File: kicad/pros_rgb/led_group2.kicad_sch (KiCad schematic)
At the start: 4 parts

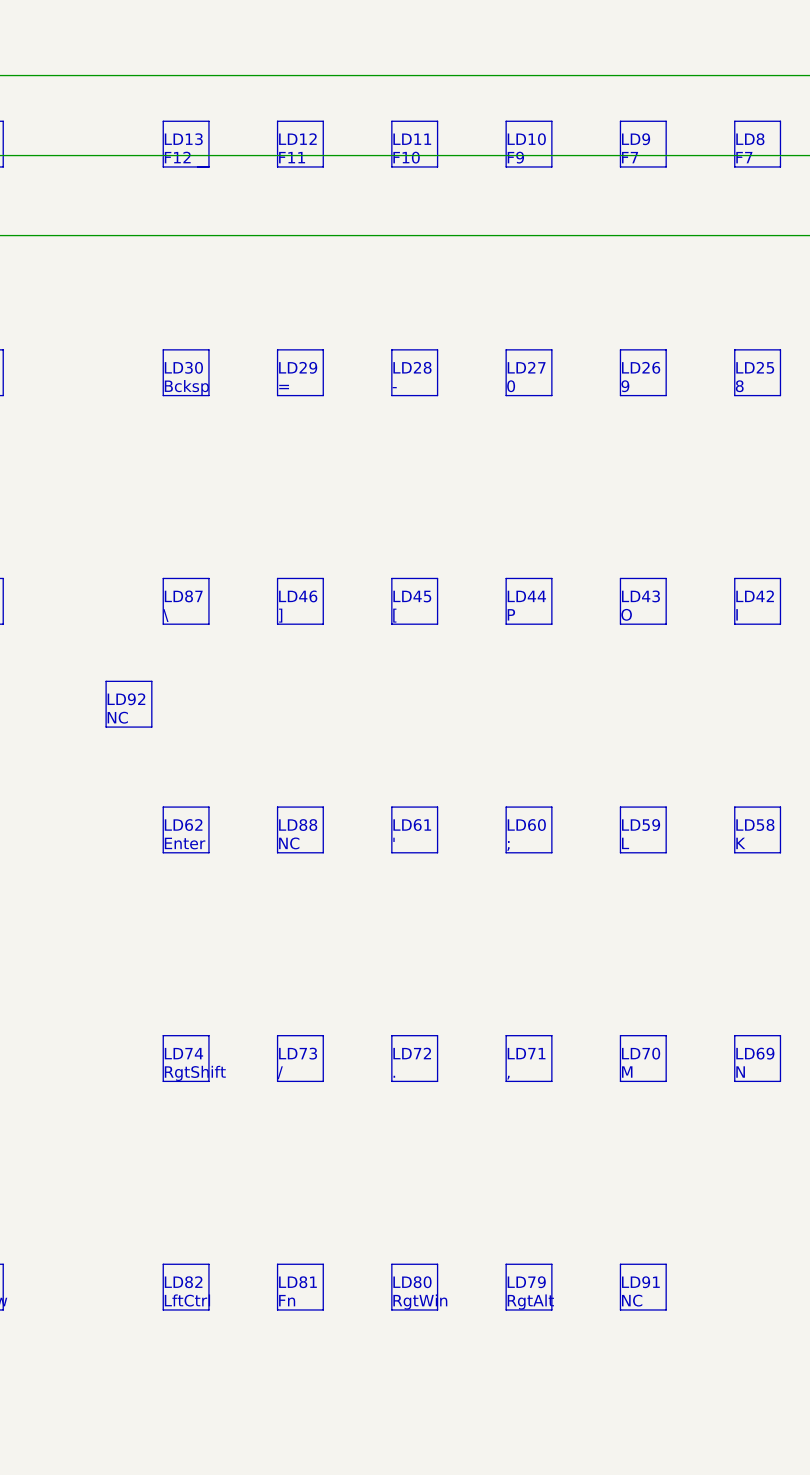
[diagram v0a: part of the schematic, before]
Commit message: kicad/pros_rgb: fix typos
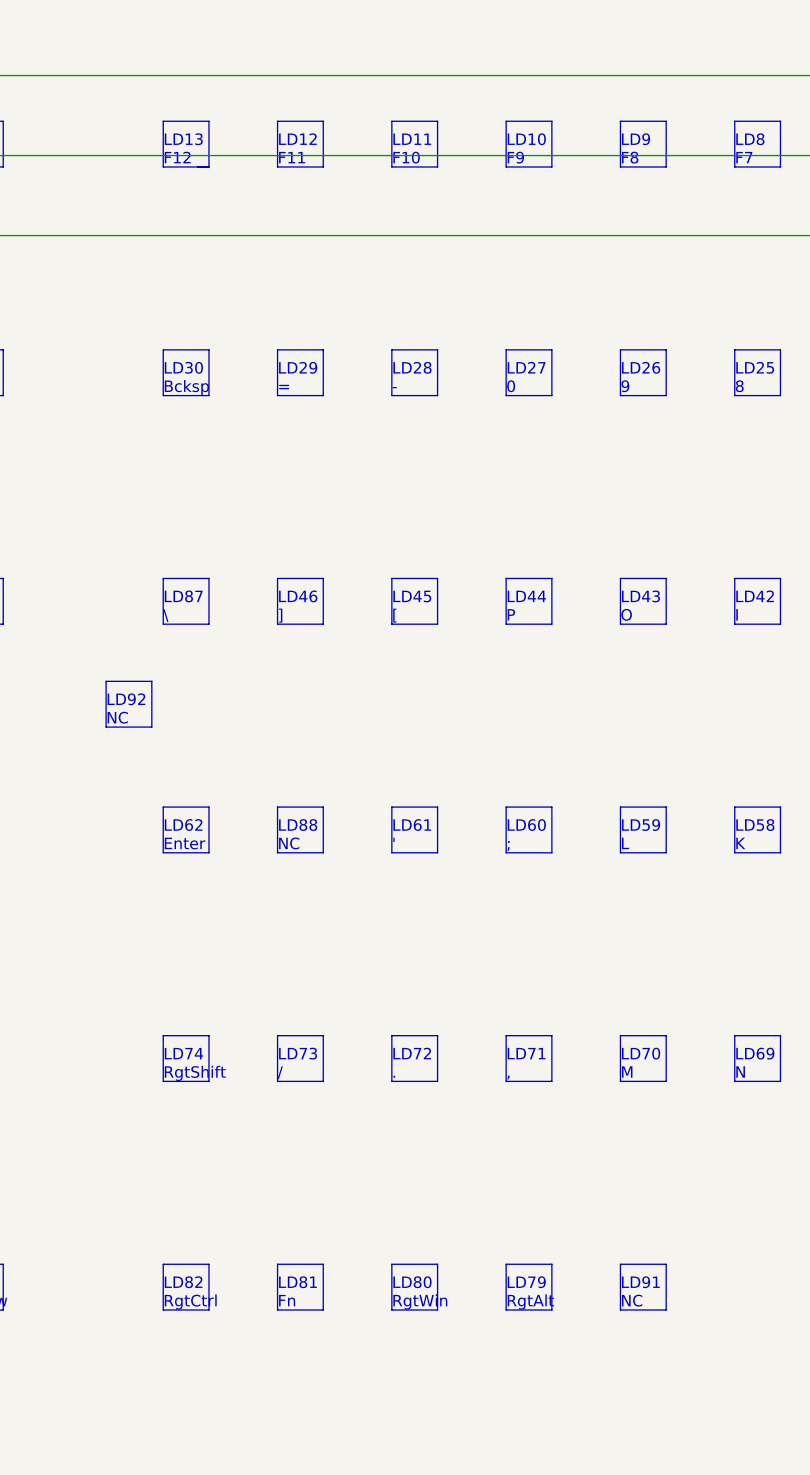
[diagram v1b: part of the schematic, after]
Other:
- note added: "LD82 RgtCtrl"
- note added: "LD9 F8"
- note removed: "LD82 LftCtrl"
- note removed: "LD9 F7"
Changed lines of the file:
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@@
     (effects (font (size 1.27 1.27)) (justify left bottom))
   )
-  (text "LD82\nLftCtrl" (at 106.68 156.21 0)
+  (text "LD82\nRgtCtrl" (at 106.68 156.21 0)
     (effects (font (size 1.27 1.27)) (justify left bottom))
   )
@@
     (effects (font (size 1.27 1.27)) (justify left bottom))
   )
-  (text "LD9\nF7" (at 157.48 29.21 0)
+  (text "LD9\nF8" (at 157.48 29.21 0)
     (effects (font (size 1.27 1.27)) (justify left bottom))
   )

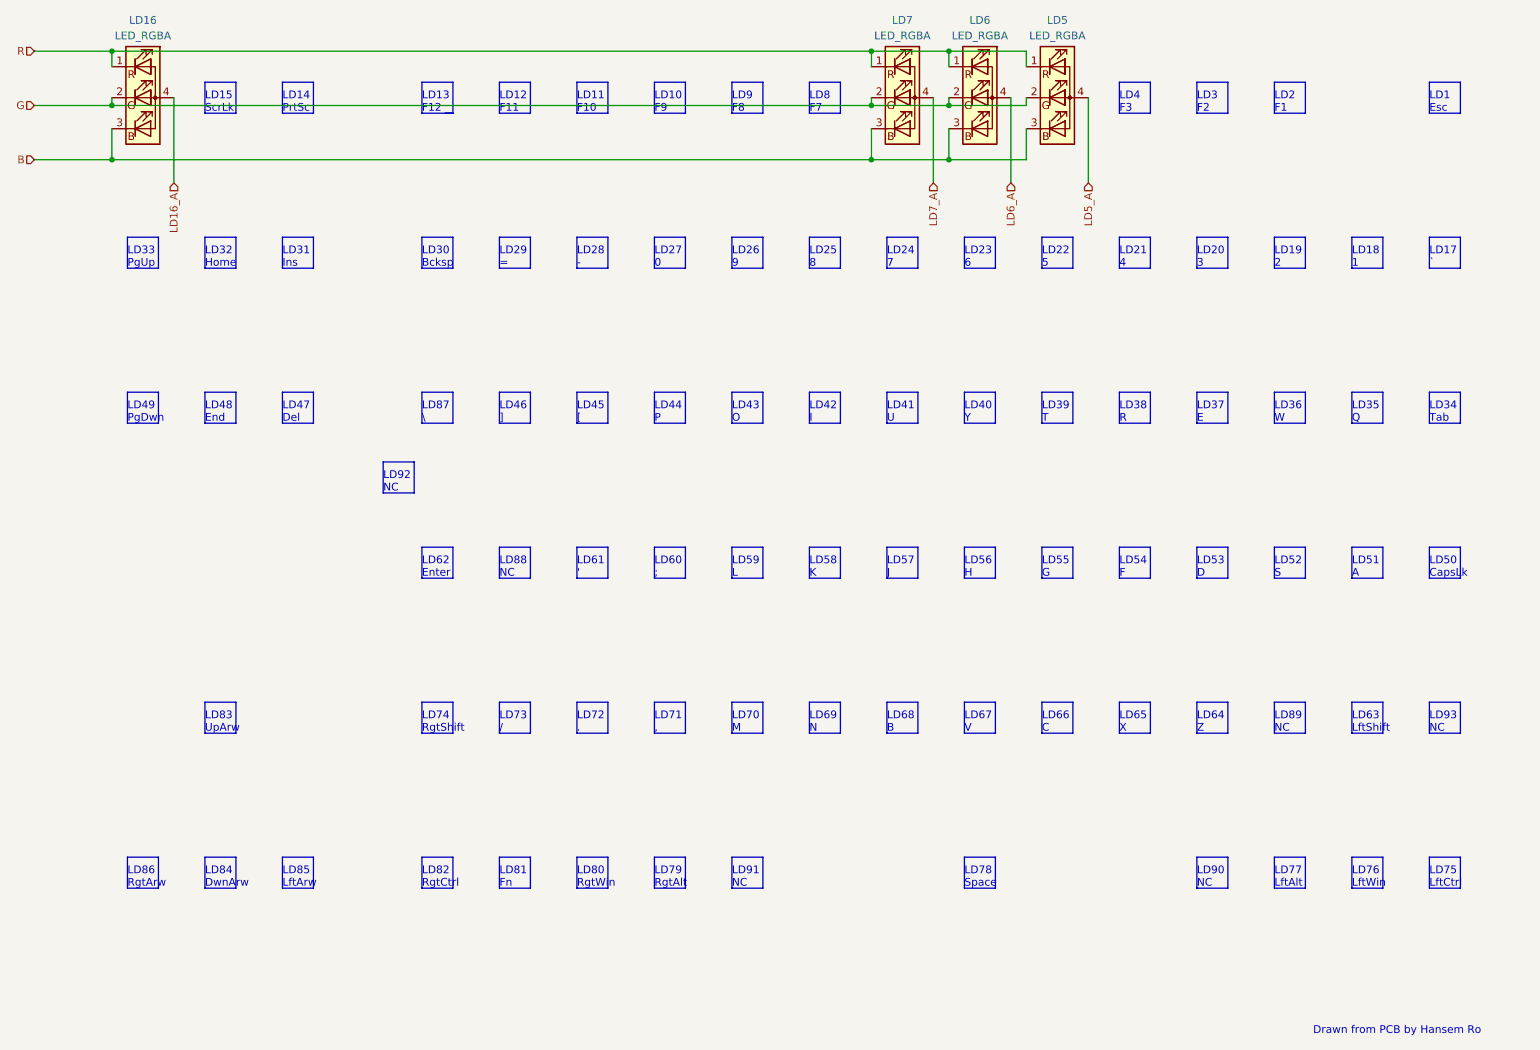
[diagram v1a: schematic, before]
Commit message: kicad/pros_rgb: order led groups by channel number
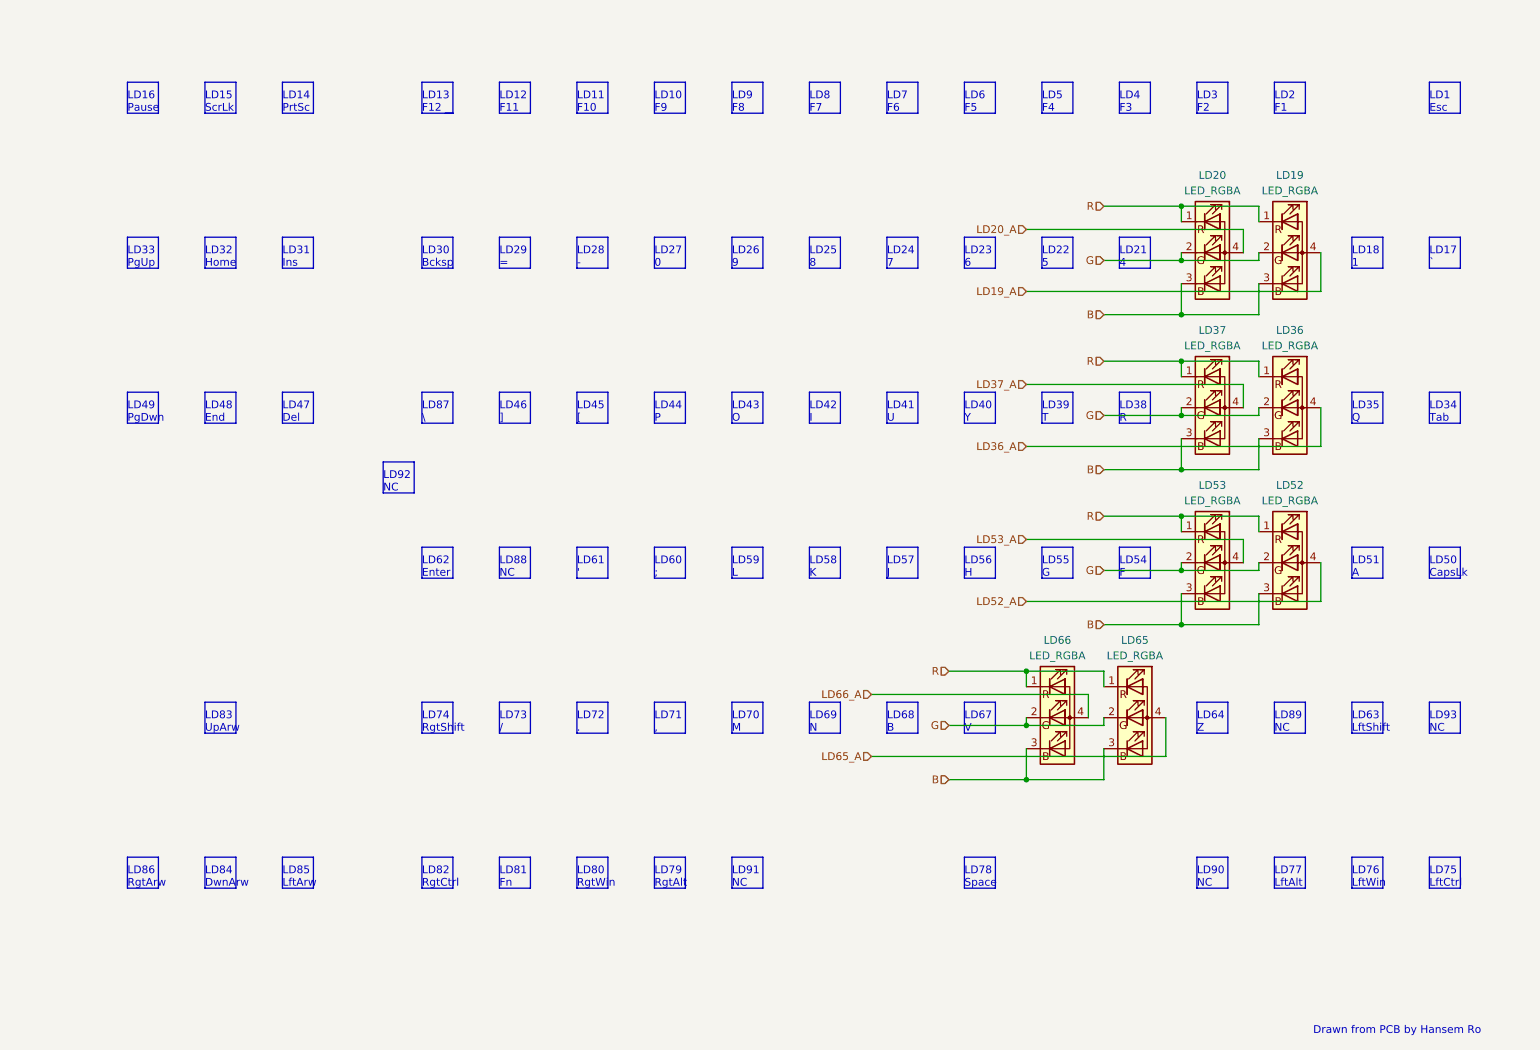
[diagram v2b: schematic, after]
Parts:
- removed LD16, LD5, LD6, LD7: LED_RGBA, symbol Device:LED_RGBA
- added LD19, LD20, LD36, LD37, LD52, LD53, LD65, LD66: LED_RGBA, symbol Device:LED_RGBA
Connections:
- net B: now also LD19.3 (BK), LD20.3 (BK), LD36.3 (BK), LD37.3 (BK), LD52.3 (BK), LD53.3 (BK), LD65.3 (BK), LD66.3 (BK)
- net G: now also LD19.2 (GK), LD20.2 (GK), LD36.2 (GK), LD37.2 (GK), LD52.2 (GK), LD53.2 (GK), LD65.2 (GK), LD66.2 (GK)
- net R: now also LD19.1 (RK), LD20.1 (RK), LD36.1 (RK), LD37.1 (RK), LD52.1 (RK), LD53.1 (RK), LD65.1 (RK), LD66.1 (RK)
- new net LD19_A: LD19.4 (A)
- new net LD20_A: LD20.4 (A)
- new net LD36_A: LD36.4 (A)
- new net LD37_A: LD37.4 (A)
- new net LD52_A: LD52.4 (A)
- new net LD53_A: LD53.4 (A)
- new net LD65_A: LD65.4 (A)
- new net LD66_A: LD66.4 (A)
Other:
- note added: "LD16 Pause"
- note added: "LD5 F4"
- note added: "LD6 F5"
- note added: "LD7 F6"
- note removed: "LD19 2"
- note removed: "LD20 3"
- note removed: "LD36 W"
- note removed: "LD37 E"
- note removed: "LD52 S"
- note removed: "LD53 D"
- note removed: "LD65 X"
- note removed: "LD66 C"
